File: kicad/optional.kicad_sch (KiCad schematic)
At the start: 18 parts, among them J10 Conn_01x20_Pin, J3 Qwiic_connector, J6 SD Card slot, J7 SD Card slot, J9 Conn_01x20_Pin, U4 74LS125

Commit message: Add Nucleo64_Z80 PCB revision 1.0
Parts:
- removed R5: 10K, Resistor_SMD:R_0805_2012Metric_Pad1.20x1.40mm_HandSolder, symbol Device:R
- renumbered D5 to D3, D6 to D4, D6 to D5, J10 to J1, J9 to J2, J6 to J4, J7 to J5, R18 to R6, R20 to R7, R20 to R8
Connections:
- net BANK_SEL2 is gone; now on net GND: U4.9
- net GND: now also U4.10
- net at D1.2 (A), D2.2 (A), R2.2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: no longer U4.10
- net A18: no longer names the net of U4.8
- no-connect marks 1 -> 2
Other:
- title: (none) -> Nucleo64 Z80

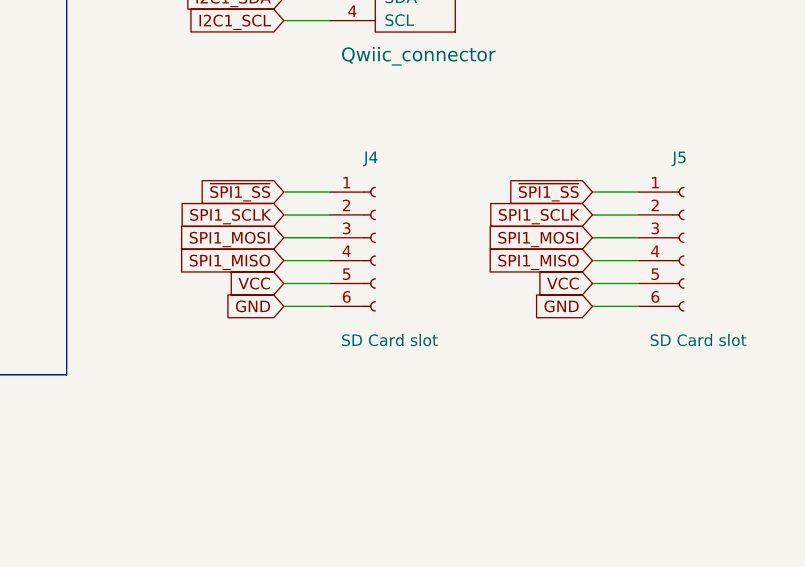
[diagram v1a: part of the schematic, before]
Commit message: Add Nucleo64_Z80 PCB revision 1.1
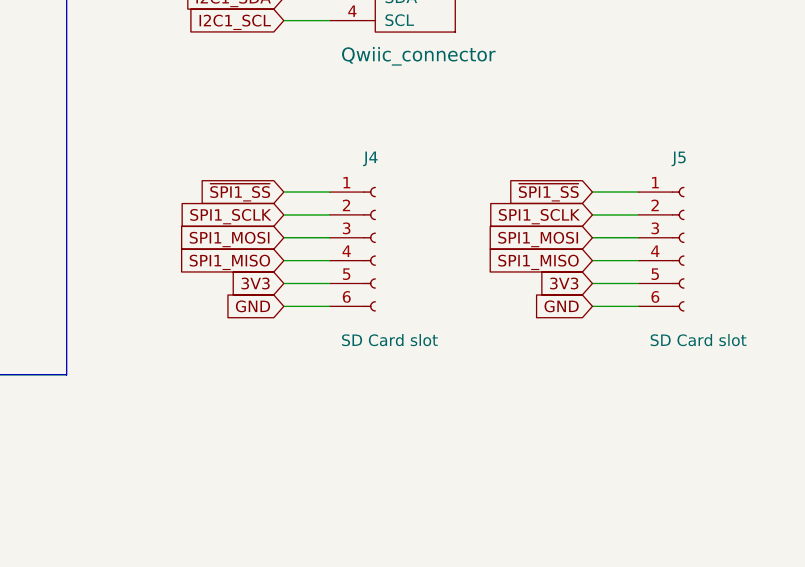
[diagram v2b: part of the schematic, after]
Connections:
- net 3V3: now also J4.5 (Pin_5), J5.5 (Pin_5)
- net VCC: no longer J4.5 (Pin_5), J5.5 (Pin_5)
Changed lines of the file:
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@@
 	(title_block
 		(title "Nucleo64 Z80")
-		(date "2024-04-29")
-		(rev "1.0")
+		(date "2024-05-18")
+		(rev "1.1")
 	)
 	(junction
@@
 		)
 	)
+	(global_label "3V3"
+		(shape input)
+		(at 245.11 148.59 180)
+		(fields_autoplaced yes)
+		(effects
+			(font
+				(size 1.27 1.27)
+			)
+			(justify right)
+		)
+		(property "Intersheetrefs" "${INTERSHEET_REFS}"
+			(at 238.6966 148.59 0)
+			(effects
+				(font
+					(size 1.27 1.27)
+				)
+				(justify right)
+				(hide yes)
+			)
+		)
+	)
 	(global_label "A16"
 		(shape output)
@@
 		)
 	)
+	(global_label "3V3"
+		(shape input)
+		(at 210.82 148.59 180)
+		(fields_autoplaced yes)
+		(effects
+			(font
+				(size 1.27 1.27)
+			)
+			(justify right)
+		)
+		(property "Intersheetrefs" "${INTERSHEET_REFS}"
+			(at 204.4066 148.59 0)
+			(effects
+				(font
+					(size 1.27 1.27)
+				)
+				(justify right)
+				(hide yes)
+			)
+		)
+	)
 	(global_label "D1"
 		(shape input)
@@
 		)
 	)
-	(global_label "VCC"
-		(shape input)
-		(at 210.82 148.59 180)
-		(fields_autoplaced yes)
-		(effects
-			(font
-				(size 1.27 1.27)
-			)
-			(justify right)
-		)
-		(property "Intersheetrefs" "${INTERSHEET_REFS}"
-			(at 204.2856 148.59 0)
-			(effects
-				(font
-					(size 1.27 1.27)
-				)
-				(justify right)
-				(hide yes)
-			)
-		)
-	)
 	(global_label "I2C1_SCL"
 		(shape input)
@@
 				(hide yes)
 			)
-		)
-	)
-	(global_label "VCC"
-		(shape input)
-		(at 245.11 148.59 180)
-		(fields_autoplaced yes)
-		(effects
-			(font
-				(size 1.27 1.27)
-			)
-			(justify right)
-		)
-		(property "Intersheetrefs" "${INTERSHEET_REFS}"
-			(at 238.5756 148.59 0)
-			(effects
-				(font
-					(size 1.27 1.27)
-				)
-				(justify right)
-				(hide yes)
-			)

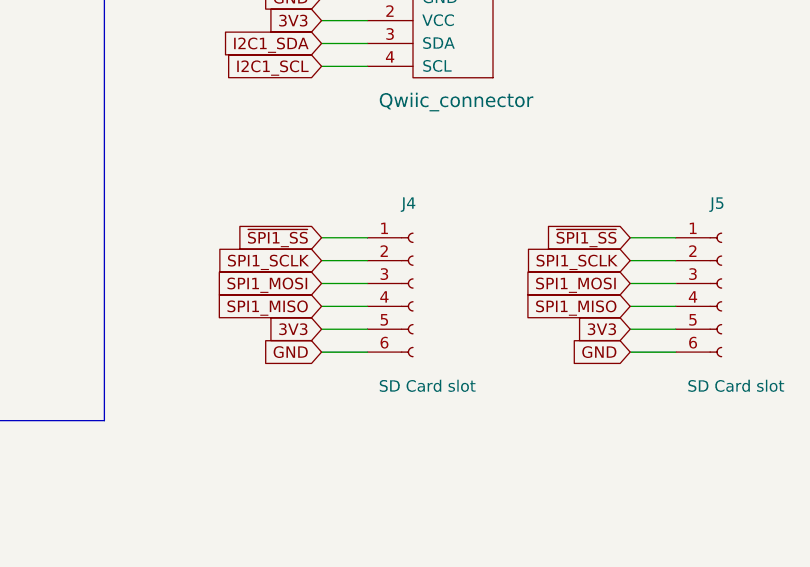
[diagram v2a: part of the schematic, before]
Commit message: Add Nucleo64_Z80 PCB revision 1.2
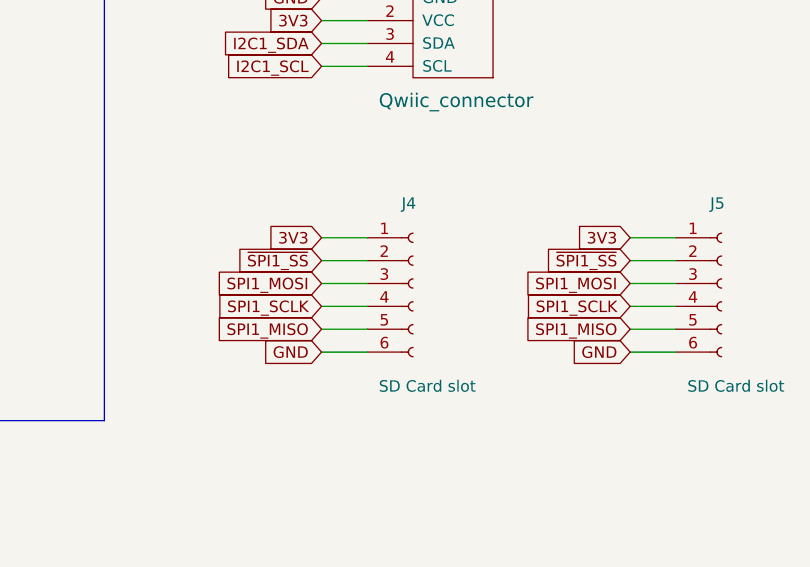
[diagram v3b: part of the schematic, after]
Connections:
- net 3V3: now also J4.1 (Pin_1), J5.1 (Pin_1); no longer J4.5 (Pin_5), J5.5 (Pin_5)
- net SPI1_MISO: now also J4.5 (Pin_5), J5.5 (Pin_5); no longer J4.4 (Pin_4), J5.4 (Pin_4)
- net SPI1_SCLK: now also J4.4 (Pin_4), J5.4 (Pin_4); no longer J4.2 (Pin_2), J5.2 (Pin_2)
- net ~{SPI1_SS}: now also J4.2 (Pin_2), J5.2 (Pin_2); no longer J4.1 (Pin_1), J5.1 (Pin_1)
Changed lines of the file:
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@@
 		(title "Nucleo64 Z80")
 		(date "2024-05-18")
-		(rev "1.1")
+		(rev "1.2")
 	)
 	(junction
@@
 	(global_label "~{SPI1_SS}"
 		(shape input)
-		(at 245.11 138.43 180)
-		(fields_autoplaced yes)
-		(effects
-			(font
-				(size 1.27 1.27)
-			)
-			(justify right)
-		)
-		(property "Intersheetrefs" "${INTERSHEET_REFS}"
-			(at 234.5238 138.43 0)
+		(at 245.11 140.97 180)
+		(fields_autoplaced yes)
+		(effects
+			(font
+				(size 1.27 1.27)
+			)
+			(justify right)
+		)
+		(property "Intersheetrefs" "${INTERSHEET_REFS}"
+			(at 234.5238 140.97 0)
 			(effects
 				(font
@@
 	(global_label "3V3"
 		(shape input)
-		(at 245.11 148.59 180)
-		(fields_autoplaced yes)
-		(effects
-			(font
-				(size 1.27 1.27)
-			)
-			(justify right)
-		)
-		(property "Intersheetrefs" "${INTERSHEET_REFS}"
-			(at 238.6966 148.59 0)
+		(at 245.11 138.43 180)
+		(fields_autoplaced yes)
+		(effects
+			(font
+				(size 1.27 1.27)
+			)
+			(justify right)
+		)
+		(property "Intersheetrefs" "${INTERSHEET_REFS}"
+			(at 238.6966 138.43 0)
 			(effects
 				(font
@@
 	(global_label "SPI1_SCLK"
 		(shape input)
-		(at 210.82 140.97 180)
-		(fields_autoplaced yes)
-		(effects
-			(font
-				(size 1.27 1.27)
-			)
-			(justify right)
-		)
-		(property "Intersheetrefs" "${INTERSHEET_REFS}"
-			(at 197.8752 140.97 0)
+		(at 210.82 146.05 180)
+		(fields_autoplaced yes)
+		(effects
+			(font
+				(size 1.27 1.27)
+			)
+			(justify right)
+		)
+		(property "Intersheetrefs" "${INTERSHEET_REFS}"
+			(at 197.8752 146.05 0)
 			(effects
 				(font
@@
 	(global_label "SPI1_SCLK"
 		(shape input)
-		(at 245.11 140.97 180)
-		(fields_autoplaced yes)
-		(effects
-			(font
-				(size 1.27 1.27)
-			)
-			(justify right)
-		)
-		(property "Intersheetrefs" "${INTERSHEET_REFS}"
-			(at 232.1652 140.97 0)
+		(at 245.11 146.05 180)
+		(fields_autoplaced yes)
+		(effects
+			(font
+				(size 1.27 1.27)
+			)
+			(justify right)
+		)
+		(property "Intersheetrefs" "${INTERSHEET_REFS}"
+			(at 232.1652 146.05 0)
 			(effects
 				(font
@@
 	(global_label "SPI1_MISO"
 		(shape input)
-		(at 210.82 146.05 180)
-		(fields_autoplaced yes)
-		(effects
-			(font
-				(size 1.27 1.27)
-			)
-			(justify right)
-		)
-		(property "Intersheetrefs" "${INTERSHEET_REFS}"
-			(at 198.0566 146.05 0)
+		(at 210.82 148.59 180)
+		(fields_autoplaced yes)
+		(effects
+			(font
+				(size 1.27 1.27)
+			)
+			(justify right)
+		)
+		(property "Intersheetrefs" "${INTERSHEET_REFS}"
+			(at 198.0566 148.59 0)
 			(effects
 				(font
@@
 	(global_label "SPI1_MISO"
 		(shape input)
-		(at 245.11 146.05 180)
-		(fields_autoplaced yes)
-		(effects
-			(font
-				(size 1.27 1.27)
-			)
-			(justify right)
-		)
-		(property "Intersheetrefs" "${INTERSHEET_REFS}"
-			(at 232.3466 146.05 0)
+		(at 245.11 148.59 180)
+		(fields_autoplaced yes)
+		(effects
+			(font
+				(size 1.27 1.27)
+			)
+			(justify right)
+		)
+		(property "Intersheetrefs" "${INTERSHEET_REFS}"
+			(at 232.3466 148.59 0)
 			(effects
 				(font
@@
 	(global_label "3V3"
 		(shape input)
-		(at 210.82 148.59 180)
-		(fields_autoplaced yes)
-		(effects
-			(font
-				(size 1.27 1.27)
-			)
-			(justify right)
-		)
-		(property "Intersheetrefs" "${INTERSHEET_REFS}"
-			(at 204.4066 148.59 0)
+		(at 210.82 138.43 180)
+		(fields_autoplaced yes)
+		(effects
+			(font
+				(size 1.27 1.27)
+			)
+			(justify right)
+		)
+		(property "Intersheetrefs" "${INTERSHEET_REFS}"
+			(at 204.4066 138.43 0)
 			(effects
 				(font
@@
 	(global_label "~{SPI1_SS}"
 		(shape input)
-		(at 210.82 138.43 180)
-		(fields_autoplaced yes)
-		(effects
-			(font
-				(size 1.27 1.27)
-			)
-			(justify right)
-		)
-		(property "Intersheetrefs" "${INTERSHEET_REFS}"
-			(at 200.2338 138.43 0)
-			(effects
-				(font
+		(at 210.82 140.97 180)
+		(fields_autoplaced yes)
+		(effects
+			(font
+				(size 1.27 1.27)
+			)
+			(justify right)
+		)
+		(property "Intersheetrefs" "${INTERSHEET_REFS}"
+			(at 200.2338 140.97 0)
+			(effects
+				(font
